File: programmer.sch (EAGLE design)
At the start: 20 parts, among them IC1 74ABT125DB, U1 ATMEGA8U2, X1 16MHz

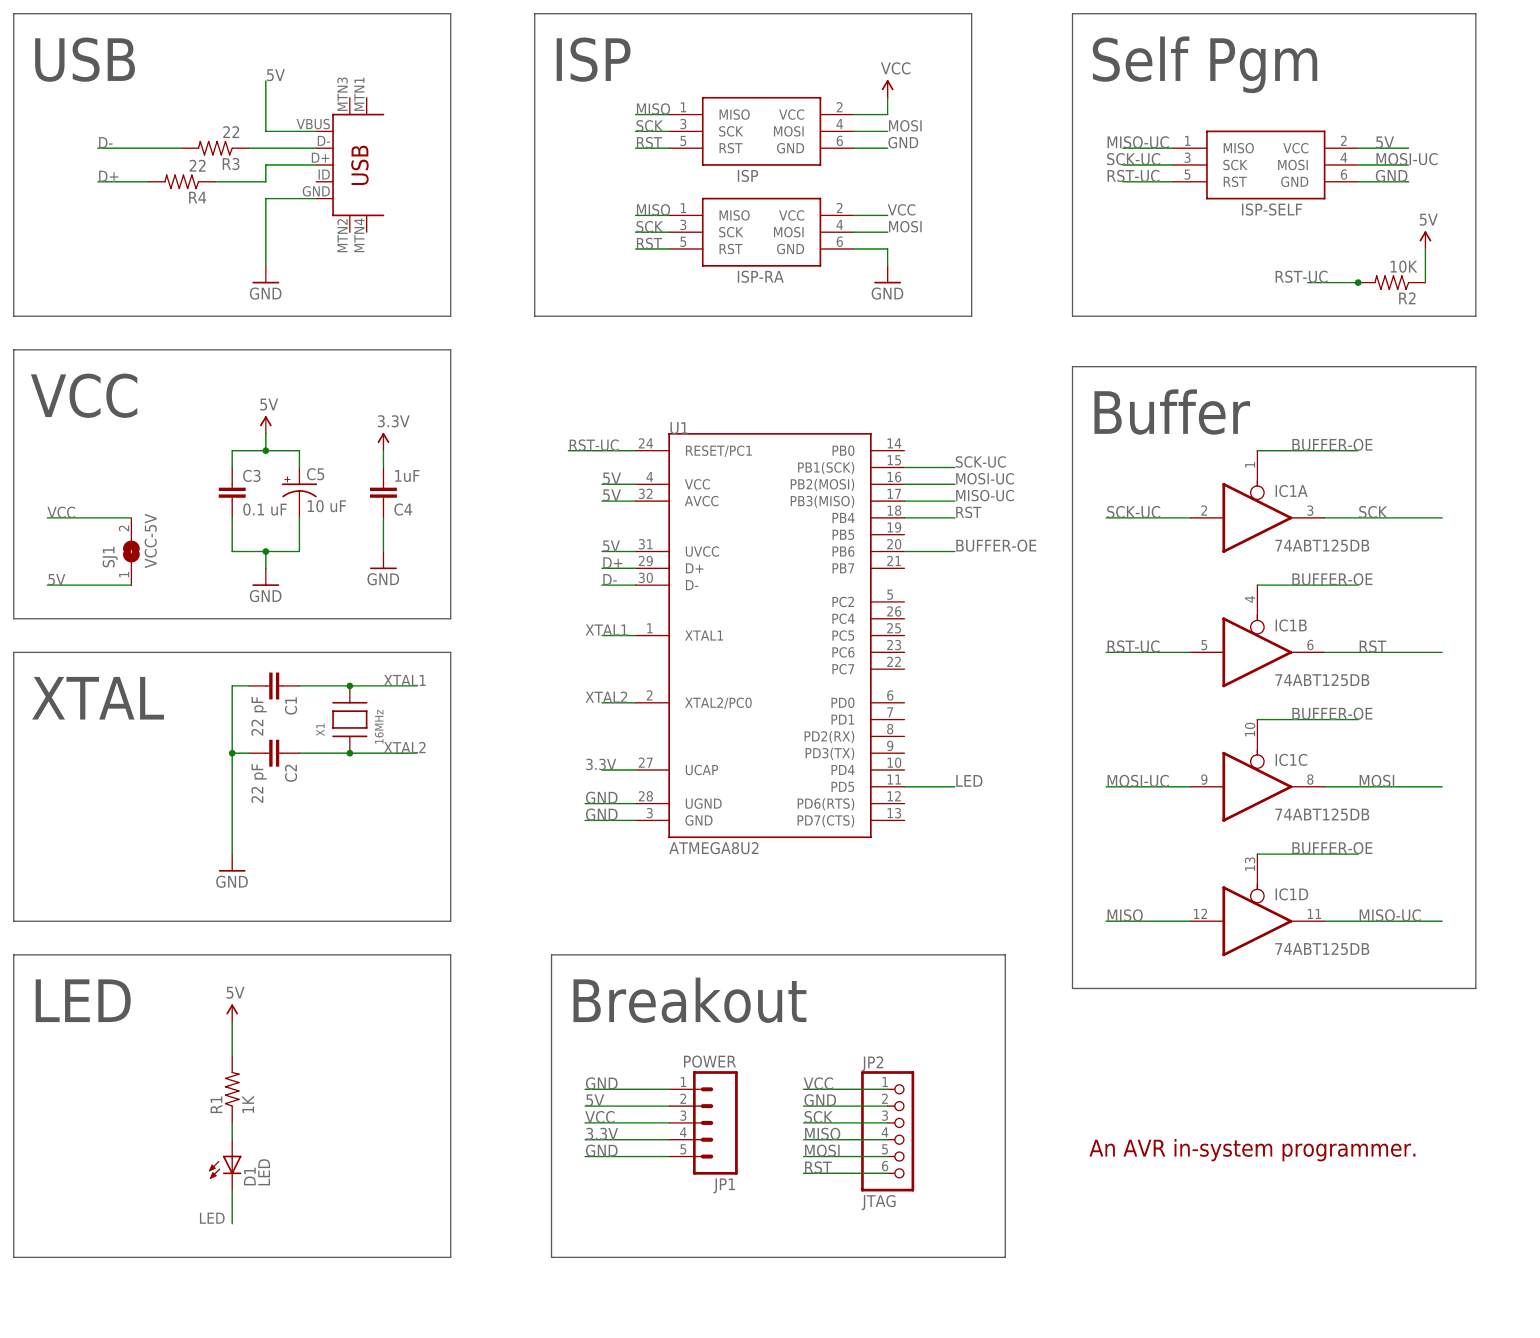
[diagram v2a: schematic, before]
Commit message: Fixed miswired RESET/RST/RST-UC.
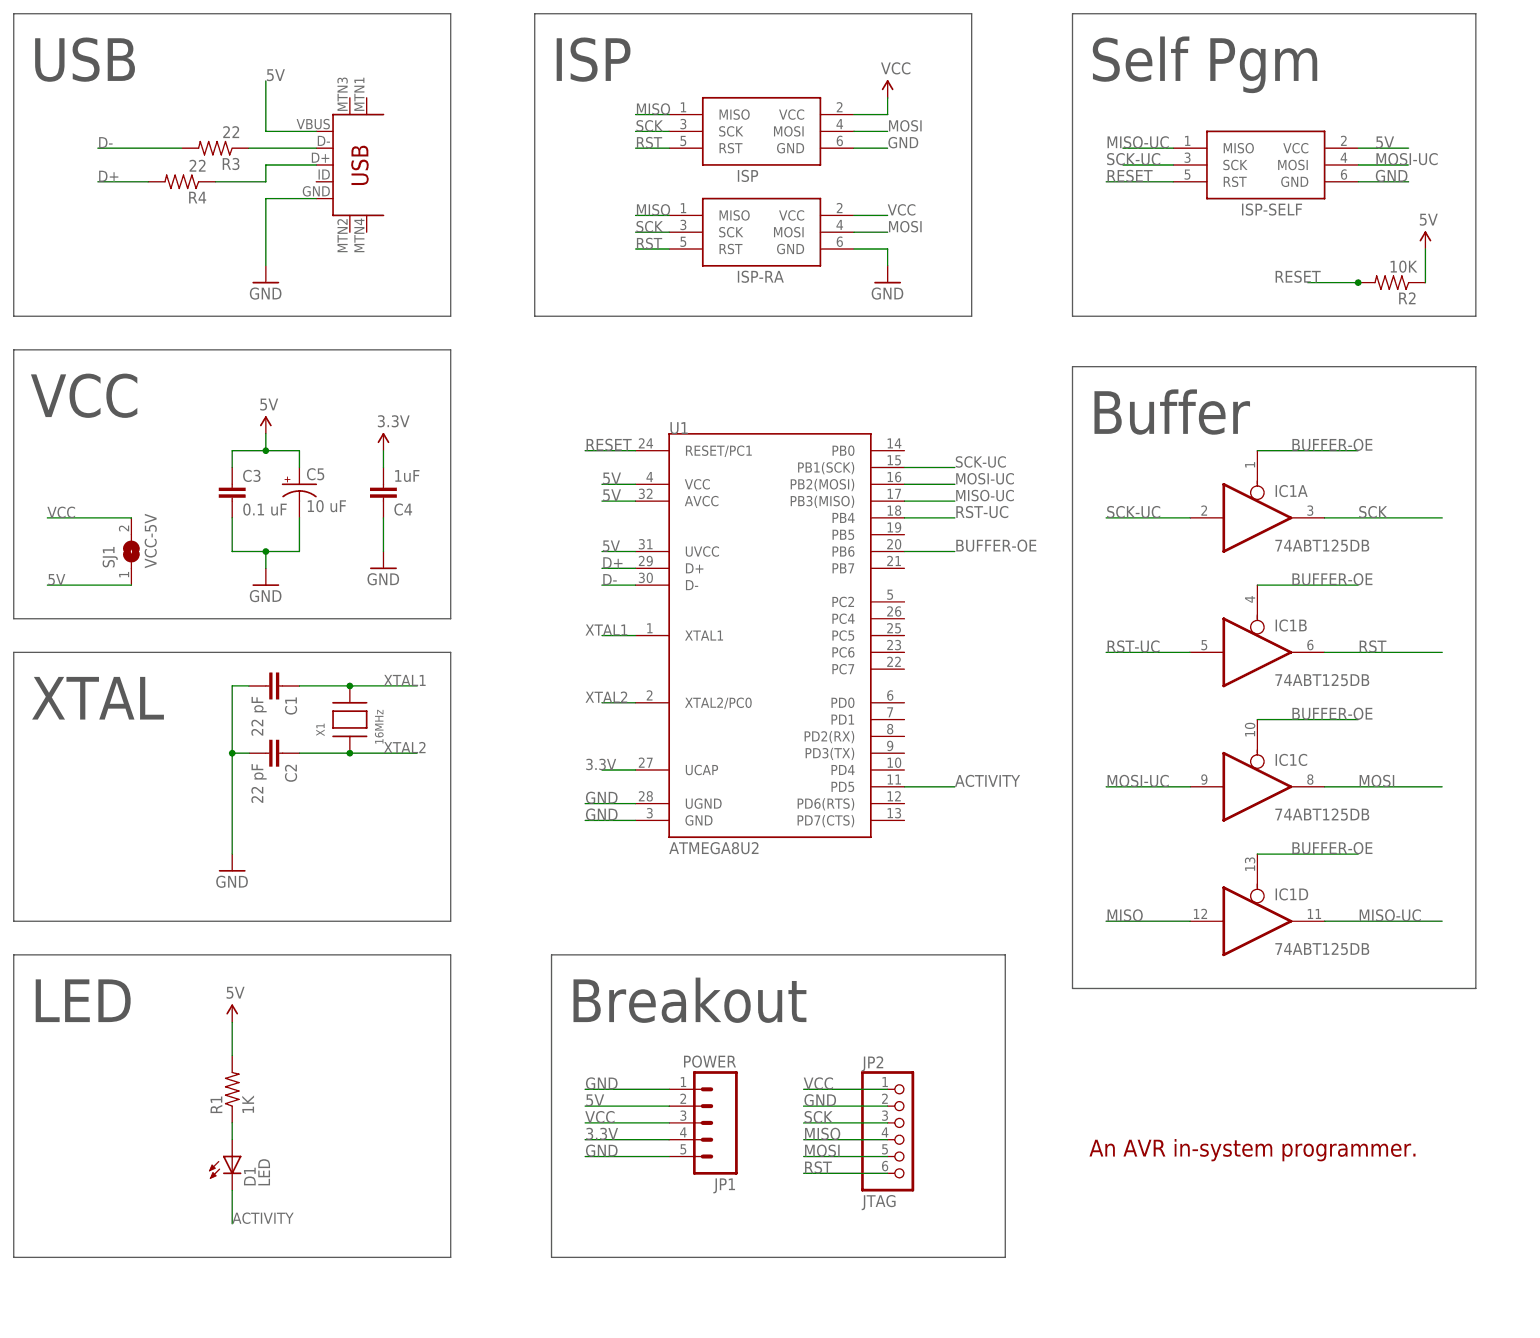
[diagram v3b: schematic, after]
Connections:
- net LED renamed ACTIVITY
- new net RESET: ISP-SELF.RST, R2.2, U1.RESET/PC1
- net RST: no longer U1.PB4
- net RST-UC: now also U1.PB4; no longer ISP-SELF.RST, R2.2, U1.RESET/PC1
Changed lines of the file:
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@@
-</segment>
-<segment>
-<pinref part="U1" gate="G$1" pin="PB4"/>
-<wire x1="73.66" y1="63.5" x2="81.28" y2="63.5" width="0.1524" layer="91"/>
-<label x="81.28" y="63.5" size="1.6764" layer="95" font="vector"/>
 </segment>
 <segment>
@@
 <net name="RST-UC" class="0">
 <segment>
-<pinref part="U1" gate="G$1" pin="RESET/PC1"/>
-<wire x1="33.02" y1="73.66" x2="22.86" y2="73.66" width="0.1524" layer="91"/>
-<label x="22.86" y="73.66" size="1.6764" layer="95" font="vector"/>
-</segment>
-<segment>
-<pinref part="R2" gate="G$1" pin="2"/>
-<label x="129.54" y="99.06" size="1.778" layer="95" font="vector"/>
-<wire x1="142.24" y1="99.06" x2="134.62" y2="99.06" width="0.1524" layer="91"/>
-<junction x="142.24" y="99.06"/>
-</segment>
-<segment>
-<pinref part="ISP-SELF" gate="G$1" pin="RST"/>
-<wire x1="114.3" y1="114.3" x2="106.68" y2="114.3" width="0.1524" layer="91"/>
-<label x="104.14" y="114.3" size="1.778" layer="95" font="vector"/>
+<pinref part="U1" gate="G$1" pin="PB4"/>
+<wire x1="73.66" y1="63.5" x2="81.28" y2="63.5" width="0.1524" layer="91"/>
+<label x="81.28" y="63.5" size="1.778" layer="95" font="vector"/>
 </segment>
 <segment>
@@
 </segment>
 </net>
-<net name="LED" class="0">
+<net name="ACTIVITY" class="0">
 <segment>
 <pinref part="D1" gate="G$1" pin="C"/>
 <wire x1="-27.94" y1="-43.18" x2="-27.94" y2="-38.1" width="0.1524" layer="91"/>
-<label x="-33.02" y="-43.18" size="1.6764" layer="95" font="vector"/>
+<label x="-27.94" y="-43.18" size="1.6764" layer="95" font="vector"/>
 </segment>
 <segment>
 <pinref part="U1" gate="G$1" pin="PD5"/>
 <wire x1="73.66" y1="22.86" x2="81.28" y2="22.86" width="0.1524" layer="91"/>
-<label x="81.28" y="22.86" size="1.778" layer="95"/>
+<label x="81.28" y="22.86" size="1.778" layer="95" font="vector"/>
 </segment>
 </net>
@@
 </segment>
 </net>
+<net name="RESET" class="0">
+<segment>
+<pinref part="R2" gate="G$1" pin="2"/>
+<label x="129.54" y="99.06" size="1.778" layer="95" font="vector"/>
+<wire x1="142.24" y1="99.06" x2="134.62" y2="99.06" width="0.1524" layer="91"/>
+<junction x="142.24" y="99.06"/>
+</segment>
+<segment>
+<pinref part="ISP-SELF" gate="G$1" pin="RST"/>
+<wire x1="114.3" y1="114.3" x2="104.14" y2="114.3" width="0.1524" layer="91"/>
+<label x="104.14" y="114.3" size="1.778" layer="95" font="vector"/>
+</segment>
+<segment>
+<pinref part="U1" gate="G$1" pin="RESET/PC1"/>
+<wire x1="33.02" y1="73.66" x2="25.4" y2="73.66" width="0.1524" layer="91"/>
+<label x="25.4" y="73.66" size="1.778" layer="95" font="vector"/>
+</segment>
+</net>

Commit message: Everything is messed up.
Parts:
- removed D1: LED, adafruit:LEDSMT1206
- removed IC1: 74ABT125DB, 74xx-us:74ABT125DB
- removed USB: USB-MINIB-5PIN, SparkFun:USB-MINIB-5PIN
- removed X1: 16MHz, adafruit:XTALNX8045
- added IC2: 74241, programmer:74241
- added JP3: TTL-SERIAL, SparkFun:M06LOCK
- added JP4: EMERGENCY CLOCK, SparkFun:M01PTH
- added JP5: HWB, SparkFun:M01PTH
- added LED1: ACTIVITY, programmer:SPARKFUN_LED
- added PDI/TPI: AVR_SPI_PRG_62X3_LOCK, SparkFun:AVR_SPI_PRG_62X3_LOCK
- added R5: 10K, SparkFun:RESISTOR0805-RES
- added X2: USB-MICROB, SparkFun:USB-MICROB
- added Y1: 16MHz, SparkFun:CRYSTAL5X3
- ISP, ISP-RA, ISP-SELF: value AVRISP-6 -> AVR_SPI_PRG_62X3_LOCK; device adafruit:AVRISP-6 -> SparkFun:AVR_SPI_PRG_62X3_LOCK
- JP1: device SparkFun:M05PTH -> SparkFun:M03LOCK
- JP2: device adafruit:PINHD-1X6 -> SparkFun:M06LOCK
- SJ1: device jumper:SJ -> SparkFun:SOLDERJUMPERNC
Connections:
- removed net MISO: IC1D.I, ISP-RA.MISO, ISP.MISO, JP2.4
- removed net MISO-UC: IC1D.O, ISP-SELF.MISO, U1.PB3(MISO)
- removed net MOSI: IC1C.O, ISP-RA.MOSI, ISP.MOSI, JP2.5
- removed net MOSI-UC: IC1C.I, ISP-SELF.MOSI, U1.PB2(MOSI)
- removed net RESET: ISP-SELF.RST, R2.2, U1.RESET/PC1
- removed net RST: IC1B.O, ISP-RA.RST, ISP.RST, JP2.6
- removed net RST-UC: IC1B.I, U1.PB4
- removed net SCK: IC1A.O, ISP-RA.SCK, ISP.SCK, JP2.3
- removed net SCK-UC: IC1A.I, ISP-SELF.SCK, U1.PB1(SCK)
- new net /HWB: JP5.1, R5.2, U1.PD7(CTS)
- new net /RESET: ISP-SELF.5, R2.2, U1.RESET/PC1
- new net CTS: JP3.5, U1.PB5
- new net ECLK: JP4.1, U1.PC6
- new net MISO/TDO: ISP-RA.1, ISP-SELF.1, ISP.1, JP2.4, U1.PB3(MISO)
- new net MOSI/TDI: IC2A.A3, ISP-SELF.4, U1.PB2(MOSI)
- new net MOSI/TDI-B: IC2A.Y3, ISP-RA.4, ISP.4, JP2.5
- new net RST/TMS/DTR: IC2A.A2, U1.PB4
- new net RST/TMS/DTR-B: IC2A.Y2, ISP-RA.5, ISP.5, JP2.6, JP3.1
- new net RXI: JP3.2, U1.PD2(RX)
- new net SCK/TCK: IC2A.A1, ISP-SELF.3, U1.PB1(SCK)
- new net SCK/TCK-B: IC2A.Y1, ISP-RA.3, ISP.3, JP2.3
- new net TXO: IC2A.A4, U1.PD3(TX)
- new net TXO-B: IC2A.Y4, JP3.3
- net 3.3V: now also JP1.3; no longer JP1.4
- net 5V: now also ISP-SELF.2, JP1.1, R5.1, X2.VBUS; no longer ISP-SELF.VCC, JP1.2, USB.VBUS
- net ACTIVITY: now also LED1.C; no longer D1.C
- net BUFFER-OE: now also IC2A.G, IC2B.G; no longer IC1A.OE, IC1B.OE, IC1C.OE, IC1D.OE
- net D+RAW: now also X2.D+; no longer USB.D+
- net D-RAW: now also X2.D-; no longer USB.D-
- net GND: now also ISP-RA.6, ISP-SELF.6, ISP.6, JP3.6, X2.GND; no longer ISP-RA.GND, ISP-SELF.GND, ISP.GND, JP1.1, JP1.5, USB.GND
- net VCC: now also ISP-RA.2, ISP.2, JP1.2, JP3.4; no longer ISP-RA.VCC, ISP.VCC, JP1.3
- net VCC-LED: now also LED1.A; no longer D1.A
- net XTAL1: now also Y1.2; no longer X1.P$2
- net XTAL2: now also Y1.1; no longer X1.P$1
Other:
- note added: "ATmegaXXU2"
- note added: "Micro USB connector might not exist in real life"
- note added: "PDI/TPI functionality is incomplete"
- note added: "TODO: hook this up to PDI"
- moved on the sheet: C1, C2, C3, C4, C5, R1, R2, R3, R4, U1
